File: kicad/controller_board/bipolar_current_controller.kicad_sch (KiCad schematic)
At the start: 92 parts, among them J1 Error signal, J2 Set point, J4 Monitor, J5 Conn_02x04_Counter_Clockwise, J6 Enable, J7 N-MOS, J8 P-MOS, J9 Shunt resistor, U1 AD8421, U19 FOD8482TR2, U2 AD8421, U3 AD8421, U4 OPA388, U5 LT1363, U6 LT1363, U7 BUF634A, U8 BUF634A

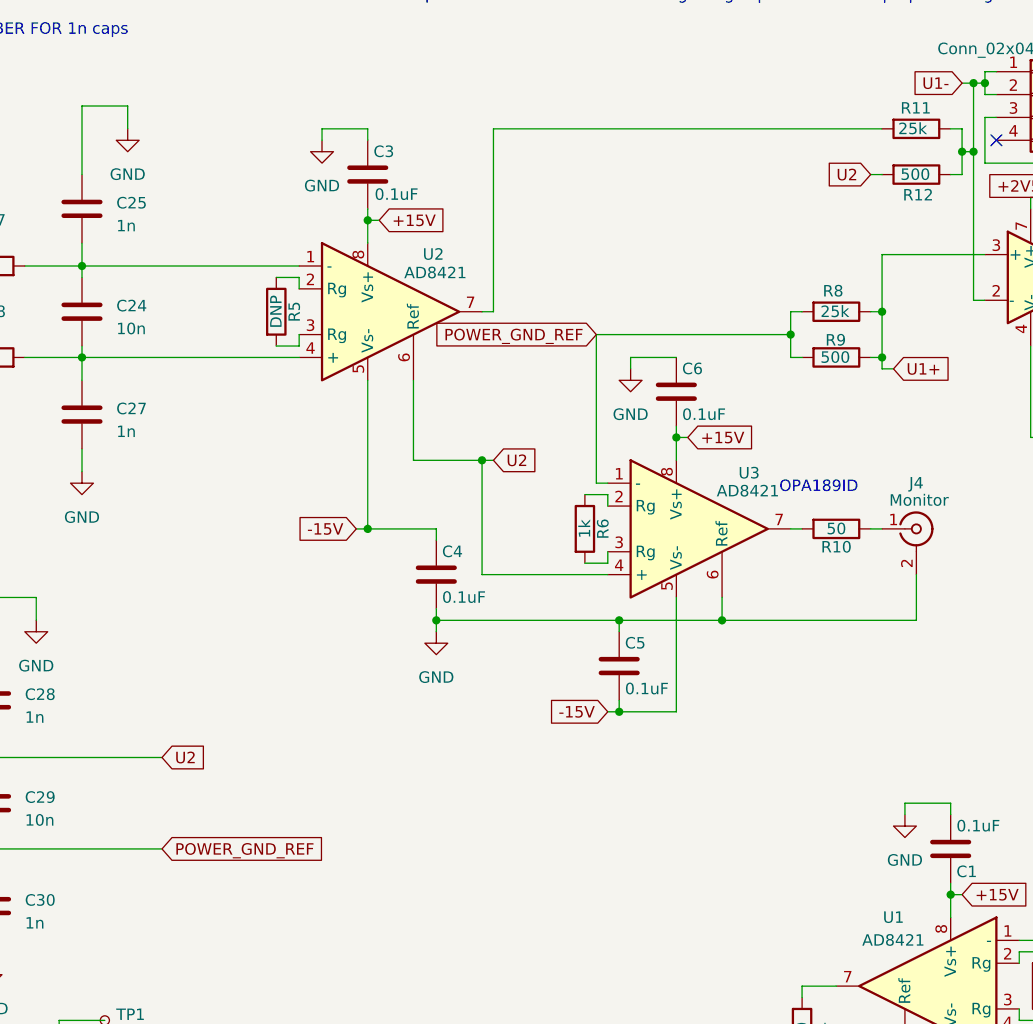
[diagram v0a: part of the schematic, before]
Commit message: Fixing wrong labels and adding silkscreen
While testing the board we discovered a wrong labeling for the
 shunt resistor terminals. The board layout is not affected by
 the wrong labeling but a silkscreen needed to be moved.

The schematic was also updated showing a clearer (and correct) labeling.

Additionally I added a legend to the board silkscreen showing the
pinout of the DIL socket.
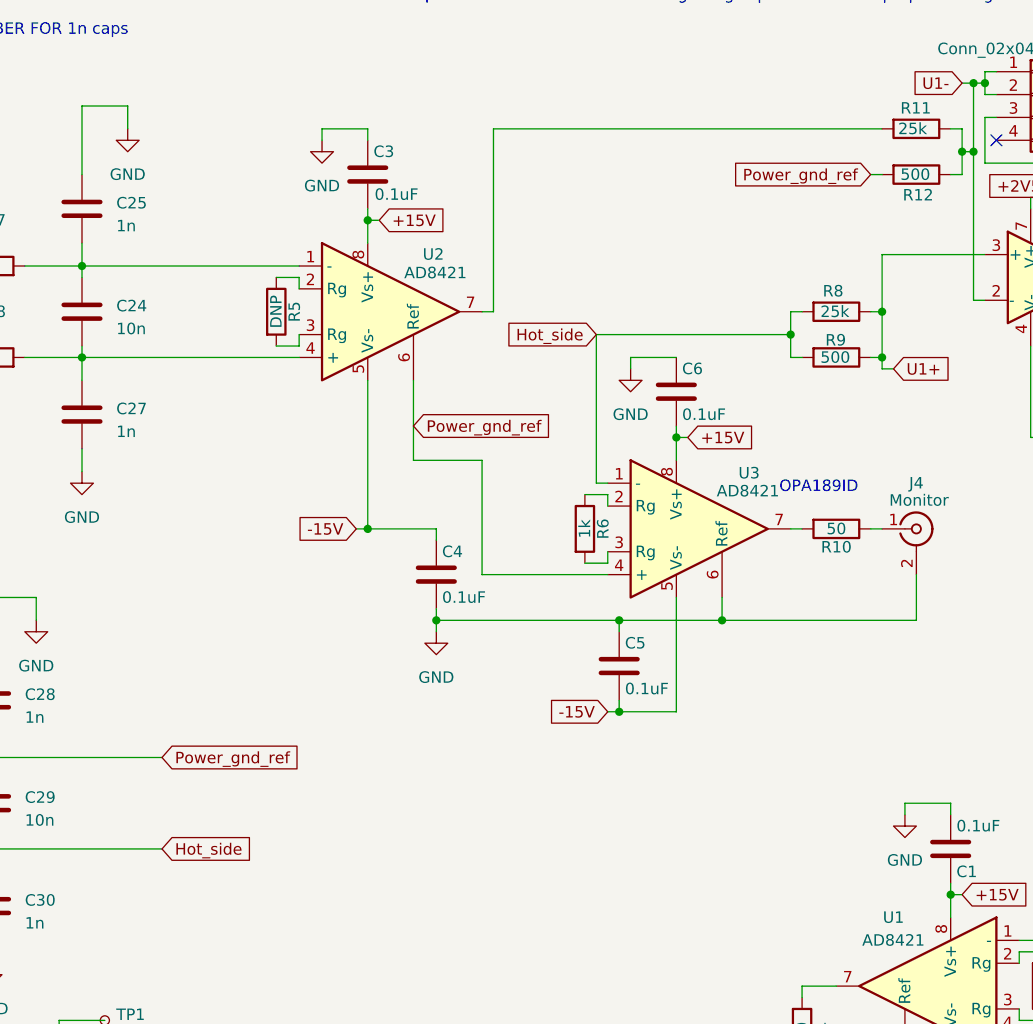
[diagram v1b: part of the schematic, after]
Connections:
- net POWER_GND_REF renamed Hot_side
- net U2 renamed Power_gnd_ref
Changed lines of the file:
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@@
   (junction (at 222.25 154.94) (diameter 0) (color 0 0 0 0)
-  )
-  (junction (at 105.41 172.72) (diameter 0) (color 0 0 0 0)
   )
   (junction (at 243.84 106.68) (diameter 0) (color 0 0 0 0)
@@
     (stroke (width 0) (type default))
   )
-  (wire (pts (xy 105.41 172.72) (xy 106.68 172.72))
-    (stroke (width 0) (type default))
-  )
   (wire (pts (xy 243.84 106.68) (xy 243.84 78.74))
     (stroke (width 0) (type default))
@@
     )
   )
-  (global_label "U2" (shape input) (at 106.68 172.72 0) (fields_autoplaced)
-    (effects (font (size 1.27 1.27)) (justify left))
-    (property "Intersheetrefs" "${INTERSHEET_REFS}" (at 111.6331 172.7994 0)
-      (effects (font (size 1.27 1.27)) (justify left) hide)
-    )
-  )
-  (global_label "POWER_GND_REF" (shape input) (at 69.85 215.9 0) (fields_autoplaced)
-    (effects (font (size 1.27 1.27)) (justify left))
-    (property "Intersheetrefs" "${INTERSHEET_REFS}" (at 88.54 215.9 0)
+  (global_label "Power_gnd_ref" (shape input) (at 97.79 168.91 0) (fields_autoplaced)
+    (effects (font (size 1.27 1.27)) (justify left))
+    (property "Intersheetrefs" "${INTERSHEET_REFS}" (at 114.3028 168.91 0)
+      (effects (font (size 1.27 1.27)) (justify left) hide)
+    )
+  )
+  (global_label "Hot_side" (shape input) (at 69.85 215.9 0) (fields_autoplaced)
+    (effects (font (size 1.27 1.27)) (justify left))
+    (property "Intersheetrefs" "${INTERSHEET_REFS}" (at 80.7991 215.9 0)
       (effects (font (size 1.27 1.27)) (justify left) hide)
     )
@@
     )
   )
-  (global_label "POWER_GND_REF" (shape input) (at 118.11 158.75 180) (fields_autoplaced)
+  (global_label "Hot_side" (shape input) (at 118.11 158.75 180) (fields_autoplaced)
     (effects (font (size 1.27 1.27)) (justify right))
-    (property "Intersheetrefs" "${INTERSHEET_REFS}" (at 99.42 158.75 0)
+    (property "Intersheetrefs" "${INTERSHEET_REFS}" (at 107.1609 158.75 0)
       (effects (font (size 1.27 1.27)) (justify right) hide)
     )
@@
     )
   )
-  (global_label "U2" (shape input) (at 69.85 205.74 0) (fields_autoplaced)
-    (effects (font (size 1.27 1.27)) (justify left))
-    (property "Intersheetrefs" "${INTERSHEET_REFS}" (at 75.2958 205.74 0)
+  (global_label "Power_gnd_ref" (shape input) (at 69.85 205.74 0) (fields_autoplaced)
+    (effects (font (size 1.27 1.27)) (justify left))
+    (property "Intersheetrefs" "${INTERSHEET_REFS}" (at 86.3628 205.74 0)
       (effects (font (size 1.27 1.27)) (justify left) hide)
     )
@@
     )
   )
-  (global_label "U2" (shape input) (at 148.59 140.97 180) (fields_autoplaced)
+  (global_label "Power_gnd_ref" (shape input) (at 148.59 140.97 180) (fields_autoplaced)
     (effects (font (size 1.27 1.27)) (justify right))
-    (property "Intersheetrefs" "${INTERSHEET_REFS}" (at 143.6369 140.8906 0)
+    (property "Intersheetrefs" "${INTERSHEET_REFS}" (at 132.0772 140.97 0)
       (effects (font (size 1.27 1.27)) (justify right) hide)
     )
